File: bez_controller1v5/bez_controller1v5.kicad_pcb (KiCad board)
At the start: 4 copper layers, 98 x 57.6 mm, 75 parts, among them J1 Conn_01x03_Male, J10 IMU Conn_01x03_Female, J11 Conn_01x03_Male, J12 Conn_01x03_Male, J13 USB_B_Mini, J2 Conn_01x03_Male, J3 Conn_01x03_Male, J4 Screw_Terminal_01x02, J5 Conn_01x03_Male, J6 Conn_01x03_Male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

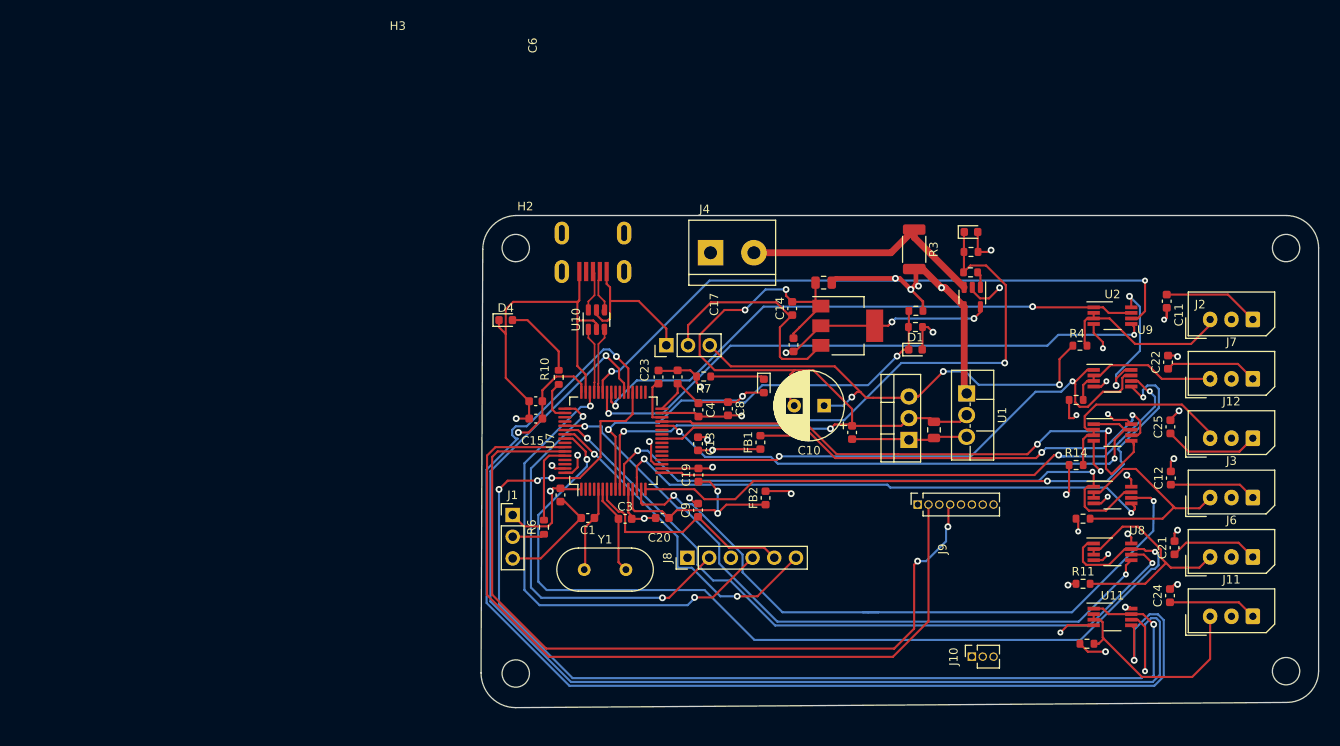
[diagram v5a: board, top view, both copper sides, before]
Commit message: fix imu footprint, adjust traces for 12V, change capacitor footprint
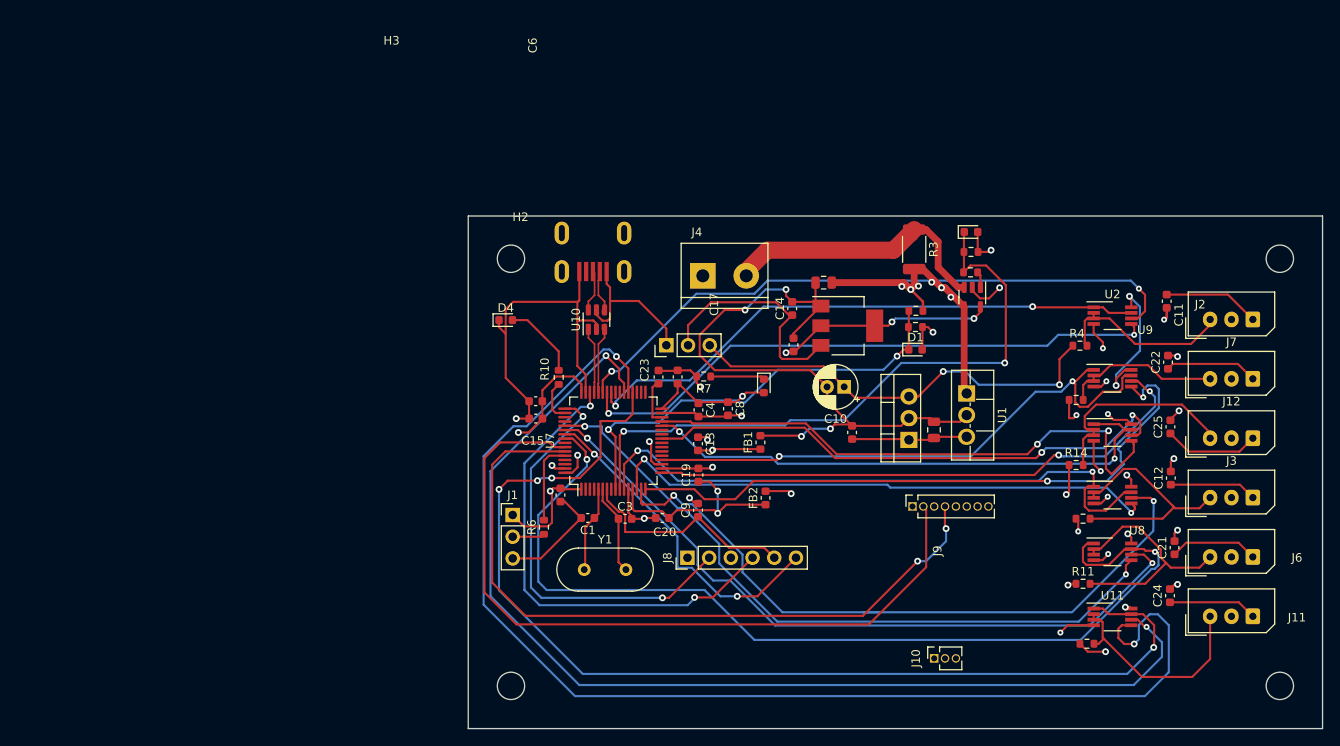
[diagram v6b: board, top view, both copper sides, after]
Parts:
- C10: footprint Capacitor_THT:CP_Radial_D8.0mm_P3.50mm -> Capacitor_THT:CP_Radial_D5.0mm_P2.00mm
- moved J10 4.42 mm to (84.5, 79.8)
- moved C10 3.22 mm to (74.0, 48.0)
- moved J4 2.85 mm to (57.5, 35.0)
- moved H3 1.87 mm to (125.0, 83.0)
- moved H1 1.55 mm to (35.0, 83.0)
- moved H4 1.45 mm to (125.0, 33.0)
- moved H2 1.37 mm to (35.0, 33.0)
- moved J9 0.64 mm to (82.0, 62.0)
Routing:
- net /USART6_RX: track 143.2 -> 129.6 mm
- net /I2C_SDA: track 95.0 -> 85.7 mm
- net /I2C_SCL: track 95.9 -> 89.4 mm
- net /PWR_GND: track 81.7 -> 76.6 mm
- net +5V: track 92.0 -> 87.1 mm, vias 14 -> 13
- net +12V: track 71.3 -> 75.5 mm, vias 10 -> 12
- net /USART6_DIR: track 132.4 -> 128.9 mm
- net /USART1_RX: track 75.4 -> 74.4 mm
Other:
- board size 98 x 57.6 mm -> 100 x 60 mm

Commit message: add headers for GPIO/buttons
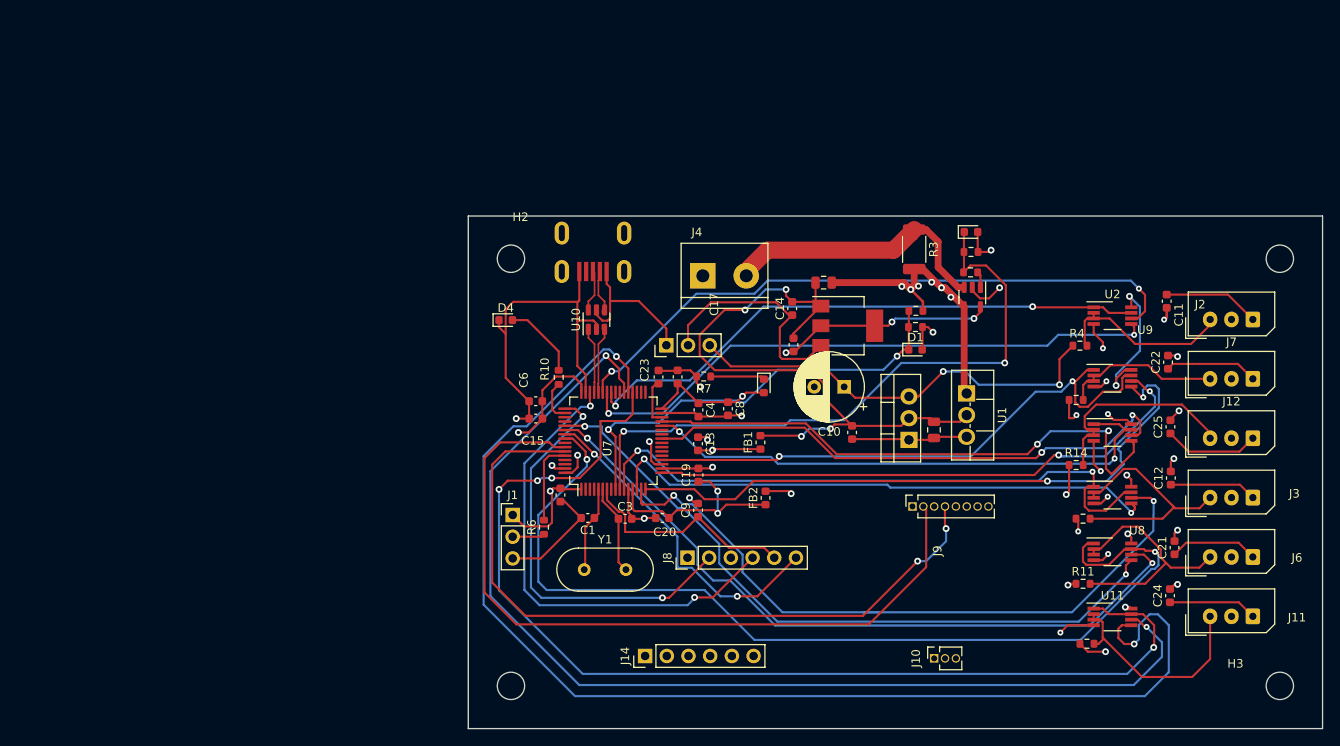
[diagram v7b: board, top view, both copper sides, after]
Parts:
- added J14: JTAG Conn_01x06_Male, Connector_PinHeader_2.54mm:PinHeader_1x06_P2.54mm_Vertical, F.Cu at (50.7, 79.5)
- C10: footprint Capacitor_THT:CP_Radial_D5.0mm_P2.00mm -> Capacitor_THT:CP_Radial_D8.0mm_P3.50mm

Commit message: routed IMU pins and minor changes
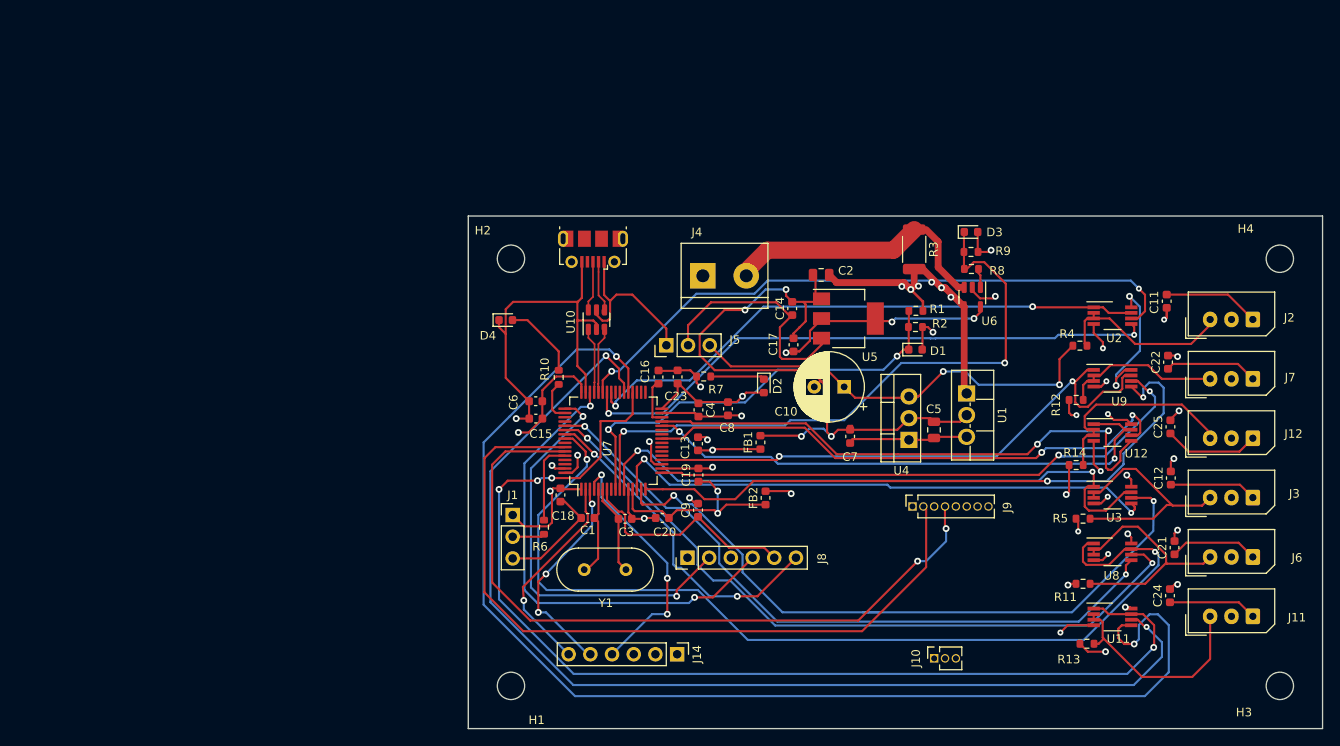
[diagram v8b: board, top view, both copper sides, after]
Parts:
- J13: footprint USB-Library:USB_MINI -> Connector_USB:USB_Micro-B_Molex-105017-0001
- moved J14 3.76 mm to (54.5, 79.3), turned to -90 degrees
- moved C2 0.95 mm to (71.3, 34.9)
- moved U5 0.85 mm to (74.5, 40.0)
- moved C7 0.51 mm to (74.7, 53.8)
- moved R8 0.41 mm to (88.9, 34.2)
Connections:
- U7 pad 2: unconnected-(U7-PC13-Pad2) -> /GPIO3
- U7 pad 3: unconnected-(U7-PC14-Pad3) -> /GPIO2
- U7 pad 4: unconnected-(U7-PC15-Pad4) -> /GPIO1
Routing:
- net /GPIO1: track 0.00 -> 30.0 mm, vias 0 -> 3
- net /GPIO2: track 0.00 -> 26.0 mm, vias 0 -> 3
- net /GPIO3: track 0.00 -> 24.8 mm, vias 0 -> 1
- net /PWR_GND: track 76.6 -> 79.0 mm
- net VBUS: track 18.1 -> 20.0 mm
- net +12V: track 75.5 -> 73.9 mm
- net /USB_CONN_D-: track 5.25 -> 6.31 mm
- net /USART3_TX: track 65.9 -> 64.8 mm
- net /USB_CONN_D+: track 4.87 -> 5.86 mm
- net /USART6_TX: track 146.4 -> 147.4 mm
- net /power: track 27.3 -> 28.2 mm
- net /MOTOR_DATA4: track 28.9 -> 28.1 mm
- net +3.3V: track 78.3 -> 79.1 mm
- net /USART2_TX: track 74.6 -> 75.2 mm
- net +5V: track 87.1 -> 86.5 mm
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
